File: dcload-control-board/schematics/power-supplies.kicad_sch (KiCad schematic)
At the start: 23 parts, among them J104 Conn_01x02_Male, U100 LMR51430YDD, U101 MC78M12A, U102 NCP718BSN330, U103 NCP718BSN500, U104 LM4040A-5.0

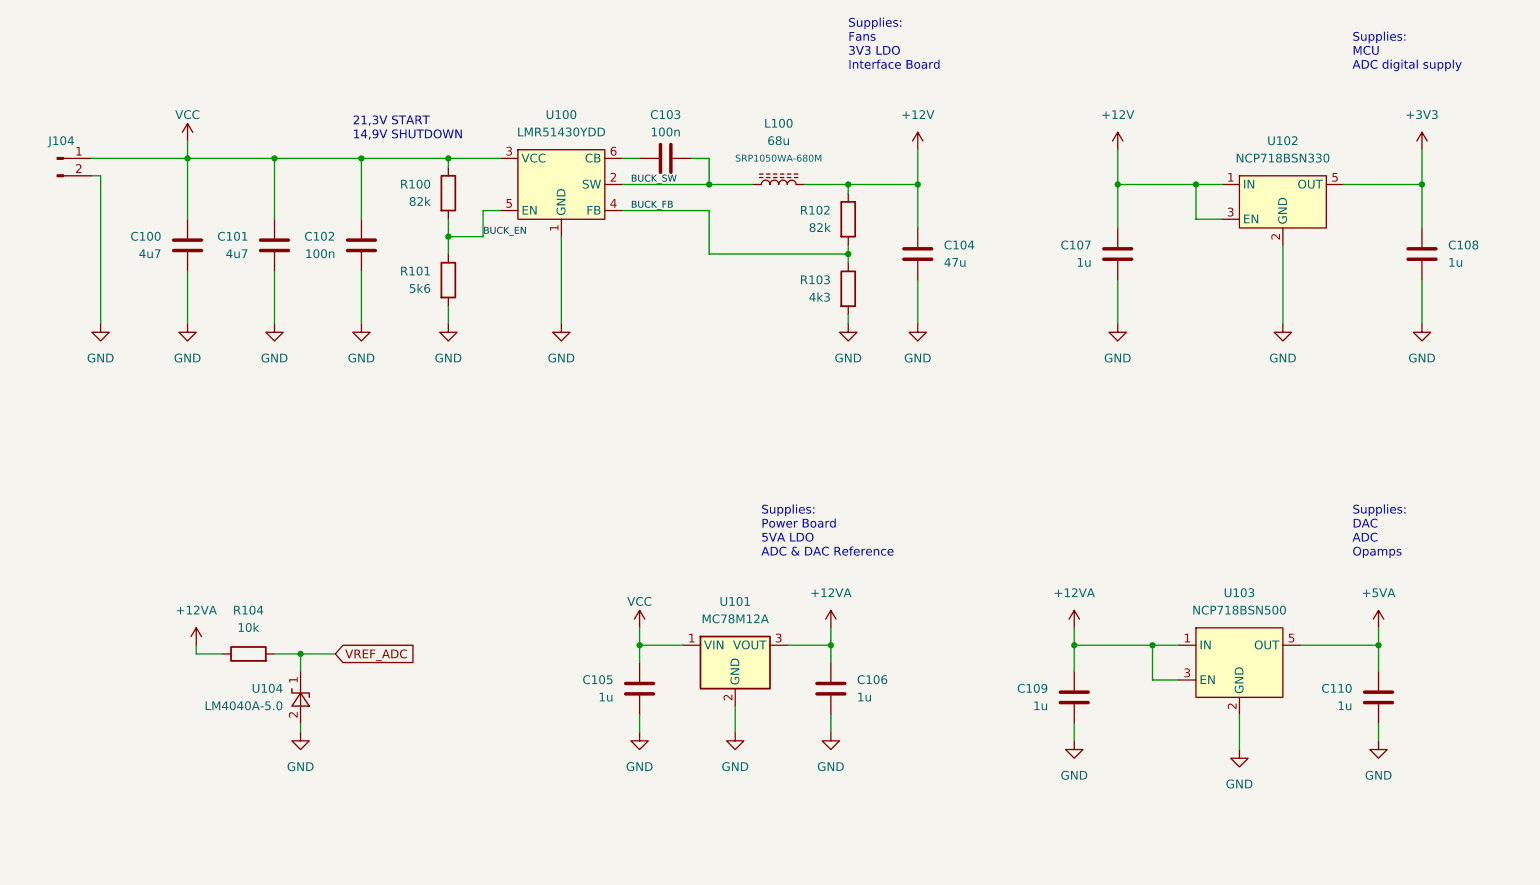
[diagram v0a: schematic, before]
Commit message: add: interface panel board
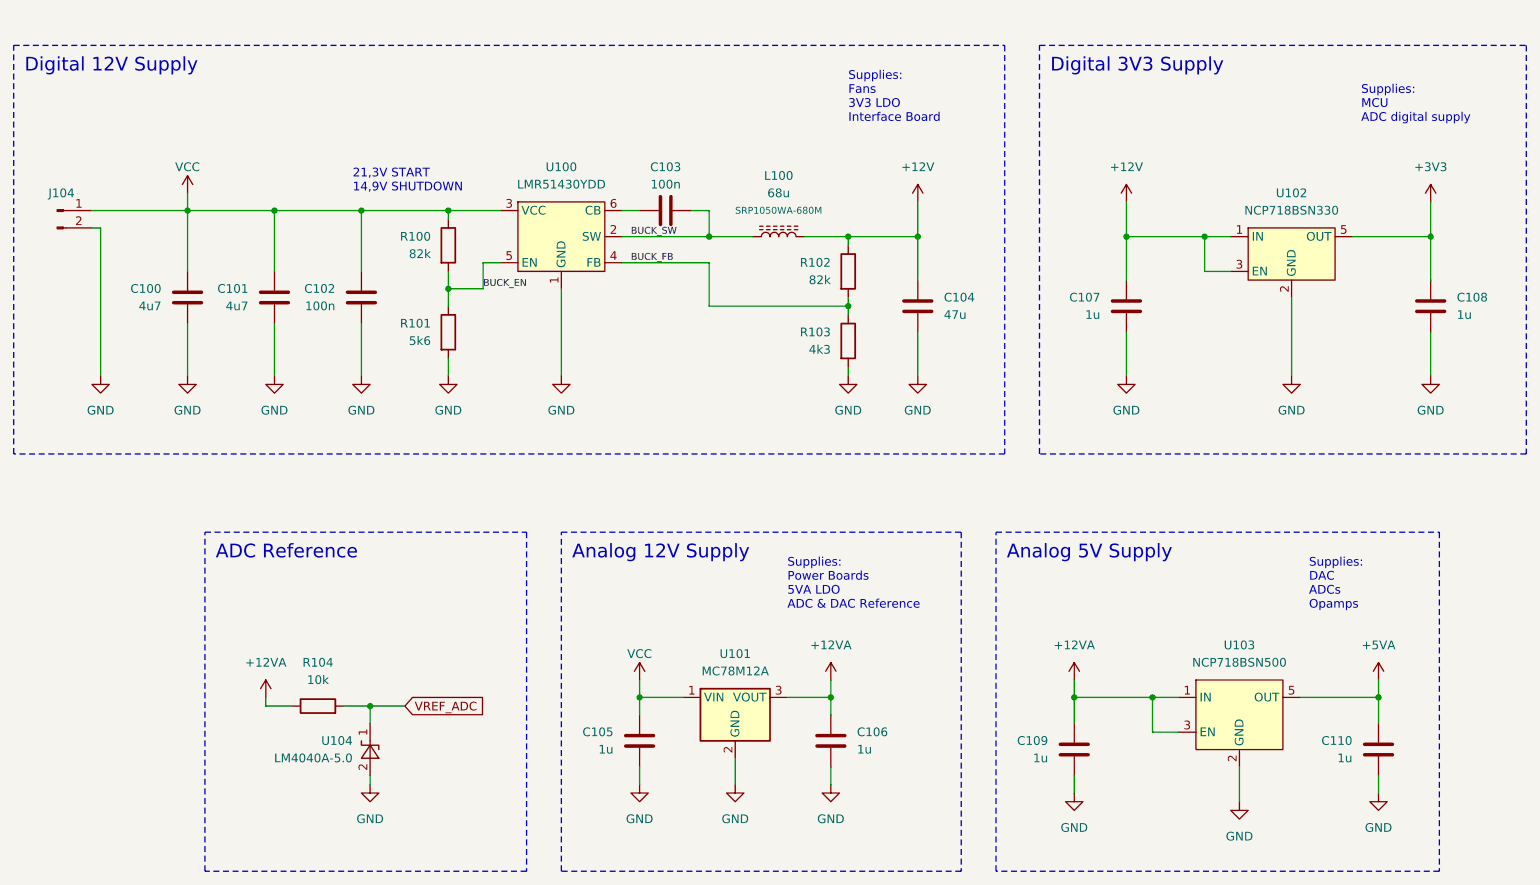
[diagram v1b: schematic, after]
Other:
- note added: "Supplies: DAC ADCs Opamps"
- note added: "Supplies: Power Boards 5VA LDO ADC & DAC Reference"
- note removed: "Supplies: DAC ADC Opamps"
- note removed: "Supplies: Power Board 5VA LDO ADC & DAC Reference"
- moved on the sheet: C100, C101, C102, C103, C104, C105, C106, C107, C108, C109, C110, J104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
